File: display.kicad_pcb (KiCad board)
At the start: 2 copper layers, 128.9 x 78.1 mm, 42 parts, among them J8 Screw_Terminal_1x04, U1 LM317T, U2 LM317T

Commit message: Beth's updated copy pre-change
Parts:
- removed B_JACK: BARREL_JACK, new-lib:Barrel_Jack
- removed C1, C3: 0.1micF, Capacitors_THT:CP_Radial_Tantal_D4.5mm_P2.50mm
- removed C2, C4: 1micF, Capacitors_THT:CP_Radial_Tantal_D4.5mm_P2.50mm
- removed Driver-to-LED (x2), Line-input (x2), Row-sink (x2): Screw_Terminal_1x08, Connectors_Terminal_Blocks:TerminalBlock_Pheonix_MPT-2.54mm_8pol
- removed J8: Screw_Terminal_1x04, Connectors_Terminal_Blocks:TerminalBlock_Pheonix_MPT-2.54mm_4pol
- removed R1, R20: 4.7k, Resistors_THT:R_Axial_DIN0204_L3.6mm_D1.6mm_P7.62mm_Horizontal
- removed R10, R11, R12, R13, R14, R15, R16, R17, R18, R21, R22, R3, R4, R5, R6, R7, R8, R9: R, Resistors_THT:R_Axial_DIN0204_L3.6mm_D1.6mm_P7.62mm_Horizontal
- removed R19, R2: 390, Resistors_THT:R_Axial_DIN0204_L3.6mm_D1.6mm_P7.62mm_Horizontal
- removed U1, U2: LM317T, new-lib:LM317T
- added 0.1uF: , Capacitors_THT:C_Disc_D7.5mm_W2.5mm_P5.00mm, F.Cu at (132.0, 97.0)
- added 0.1uF: , Capacitors_THT:C_Disc_D7.5mm_W2.5mm_P5.00mm, F.Cu at (137.0, 97.0)
- added 1uF: , Capacitors_THT:CP_Radial_D5.0mm_P2.00mm, F.Cu at (159.0, 97.0)
- added 1uF: , Capacitors_THT:CP_Radial_D5.0mm_P2.00mm, F.Cu at (149.5, 99.0)
- added 330: R, Resistors_THT:R_Axial_DIN0411_L9.9mm_D3.6mm_P5.08mm_Vertical, F.Cu at (105.6, 84.3)
- added 330: R, Resistors_THT:R_Axial_DIN0411_L9.9mm_D3.6mm_P5.08mm_Vertical, F.Cu at (76.8, 71.6)
- added 330: R, Resistors_THT:R_Axial_DIN0411_L9.9mm_D3.6mm_P5.08mm_Vertical, F.Cu at (79.3, 84.3)
- added 330: R, Resistors_THT:R_Axial_DIN0411_L9.9mm_D3.6mm_P5.08mm_Vertical, F.Cu at (81.9, 71.6)
- added 330: R, Resistors_THT:R_Axial_DIN0411_L9.9mm_D3.6mm_P5.08mm_Vertical, F.Cu at (84.4, 84.3)
- added 330: R, Resistors_THT:R_Axial_DIN0411_L9.9mm_D3.6mm_P5.08mm_Vertical, F.Cu at (87.0, 71.6)
- added 330: R, Resistors_THT:R_Axial_DIN0411_L9.9mm_D3.6mm_P5.08mm_Vertical, F.Cu at (89.5, 84.3)
- added 330: R, Resistors_THT:R_Axial_DIN0411_L9.9mm_D3.6mm_P5.08mm_Vertical, F.Cu at (92.0, 71.6)
- added 330: R, Resistors_THT:R_Axial_DIN0411_L9.9mm_D3.6mm_P5.08mm_Vertical, F.Cu at (100.5, 84.3)
- added 330: R, Resistors_THT:R_Axial_DIN0411_L9.9mm_D3.6mm_P5.08mm_Vertical, F.Cu at (103.1, 71.6)
- added 330: R, Resistors_THT:R_Axial_DIN0411_L9.9mm_D3.6mm_P5.08mm_Vertical, F.Cu at (108.1, 71.6)
- added 330: R, Resistors_THT:R_Axial_DIN0411_L9.9mm_D3.6mm_P5.08mm_Vertical, F.Cu at (110.7, 84.3)
- added 330: R, Resistors_THT:R_Axial_DIN0411_L9.9mm_D3.6mm_P5.08mm_Vertical, F.Cu at (113.2, 71.6)
- added 330: R, Resistors_THT:R_Axial_DIN0411_L9.9mm_D3.6mm_P5.08mm_Vertical, F.Cu at (115.8, 84.3)
- added 330: R, Resistors_THT:R_Axial_DIN0411_L9.9mm_D3.6mm_P5.08mm_Vertical, F.Cu at (118.3, 71.6)
- added 330: R, Resistors_THT:R_Axial_DIN0411_L9.9mm_D3.6mm_P5.08mm_Vertical, F.Cu at (74.3, 84.3)
- added 390: , Resistors_THT:R_Axial_DIN0204_L3.6mm_D1.6mm_P7.62mm_Horizontal, F.Cu at (134.0, 113.9)
- added 390: , Resistors_THT:R_Axial_DIN0204_L3.6mm_D1.6mm_P7.62mm_Horizontal, F.Cu at (126.3, 118.3)
- added 4.7k: , Resistors_THT:R_Axial_DIN0204_L3.6mm_D1.6mm_P7.62mm_Horizontal, F.Cu at (126.3, 109.4)
- added 4.7k: , Resistors_THT:R_Axial_DIN0204_L3.6mm_D1.6mm_P7.62mm_Horizontal, F.Cu at (161.0, 111.5)
- added ?: Screw_Terminal_1x04, Connectors_Terminal_Blocks:TerminalBlock_Pheonix_MPT-2.54mm_4pol, F.Cu at (173.0, 102.5)
- added ?: LM317T, Connectors_Molex:Molex_KK-6410-03_03x2.54mm_Straight, F.Cu at (127.3, 103.5)
- added ?: LM317T, Connectors_Molex:Molex_KK-6410-03_03x2.54mm_Straight, F.Cu at (160.0, 105.5)
- added ?: BARREL_JACK, Connectors:BARREL_JACK, F.Cu at (142.0, 105.5)
- added ?: 3mm drill, Wire_Pads:SolderWirePad_single_2mmDrill, F.Cu at (69.5, 57.5)
- added ?: 3mm drill hole, Wire_Pads:SolderWirePad_single_2mmDrill, F.Cu at (177.5, 57.5)
- added ?: 3mm drill hole, Wire_Pads:SolderWirePad_single_2mmDrill, F.Cu at (177.5, 118.0)
- added ?: 3mm drill hole, Wire_Pads:SolderWirePad_single_2mmDrill, F.Cu at (69.5, 118.0)
- added Driver to LEDs: Screw_Terminal_1x08, Connectors_Terminal_Blocks:TerminalBlock_Pheonix_MPT-2.54mm_8pol, F.Cu at (118.3, 62.7)
- added Driver to LEDs: Screw_Terminal_1x08, Connectors_Terminal_Blocks:TerminalBlock_Pheonix_MPT-2.54mm_8pol, F.Cu at (92.0, 62.7)
- added LEDs to Row Selector: Screw_Terminal_1x08, Connectors_Terminal_Blocks:TerminalBlock_Pheonix_MPT-2.54mm_8pol, F.Cu at (172.5, 62.7)
- added LEDs to Row Selector: Screw_Terminal_1x08, Connectors_Terminal_Blocks:TerminalBlock_Pheonix_MPT-2.54mm_8pol, F.Cu at (145.0, 62.7)
- added R: , Resistors_THT:R_Axial_DIN0204_L3.6mm_D1.6mm_P7.62mm_Horizontal, F.Cu at (153.3, 115.0)
- added R: , Resistors_THT:R_Axial_DIN0204_L3.6mm_D1.6mm_P7.62mm_Horizontal, F.Cu at (161.0, 118.5)
- added REF**: TerminalBlock_Pheonix_PT-3.5mm_2pol, Connectors_Terminal_Blocks:TerminalBlock_Pheonix_PT-3.5mm_2pol, F.Cu at (67.7, 74.8)
- added Register to Driver: Screw_Terminal_1x08, Connectors_Terminal_Blocks:TerminalBlock_Pheonix_MPT-2.54mm_8pol, F.Cu at (100.5, 114.8)
- added Register to Driver: Screw_Terminal_1x08, Connectors_Terminal_Blocks:TerminalBlock_Pheonix_MPT-2.54mm_8pol, F.Cu at (74.3, 114.8)
- moved Driver2 30.5 mm to (100.5, 105.9)
- moved Driver1 27.6 mm to (74.3, 105.9)
- moved Darlington2 16.9 mm to (154.5, 79.5)
- moved Darlington1 16.8 mm to (127.2, 79.5)
- moved Demux1 15.9 mm to (124.7, 90.9)
- moved Demux2 15.2 mm to (152.0, 91.0)
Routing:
- net GND: track 222.0 -> 166.8 mm, vias 0 -> 1
- net Net-(Demux1-Pad3): track 79.3 -> 49.8 mm, vias 2 -> 1
- net Net-(Demux1-Pad5): track 66.9 -> 43.9 mm, vias 3 -> 2
- net Net-(J5-Pad1): track 28.7 -> 8.89 mm
- net Net-(C1-Pad1): track 54.0 -> 35.0 mm
- net Net-(J5-Pad7): track 27.5 -> 8.89 mm
- net Net-(J5-Pad3): track 27.5 -> 8.89 mm
- net Net-(J5-Pad5): track 27.0 -> 8.89 mm
- net Net-(R20-Pad1): track 27.8 -> 10.0 mm, vias 1 -> 0
- net Net-(Driver1-Pad12): track 26.6 -> 8.89 mm
- net Net-(Driver1-Pad14): track 25.7 -> 8.89 mm
- net Net-(Driver1-Pad16): track 25.1 -> 8.89 mm
- net Net-(Driver1-Pad18): track 24.8 -> 8.89 mm
- net Net-(Driver1-Pad15): track 7.52 -> 21.6 mm
- net Net-(Driver1-Pad13): track 8.58 -> 21.6 mm
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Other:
- board size 128.9 x 78.1 mm -> 117 x 69.5 mm
- rule pad_to_mask_clearance: 0.2 -> 0
- board text added: "Produced by Nathan Doorly Beth Cotterell Richard Grafton"
- board text removed: "Designed by Nathan Doorly"

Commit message: Ready for manufacture
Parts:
- removed REF**: TerminalBlock_Pheonix_PT-3.5mm_2pol, Connectors_Terminal_Blocks:TerminalBlock_Pheonix_PT-3.5mm_2pol
- added GND: Screw_Terminal_1x02, Connectors_Terminal_Blocks:TerminalBlock_Pheonix_PT-3.5mm_2pol, F.Cu at (70.5, 71.3)
- 1uF (x2): value (none) -> 1micF
- 390 (x2): value (none) -> 390
- 4.7k (x2): value (none) -> 4.7k
- LED to Column: renamed from Driver to LEDs (x2)
- LED to Row: renamed from LEDs to Row Selector (x2)
- R (x2): value (none) -> R
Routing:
- net GND: track 166.8 -> 214.4 mm
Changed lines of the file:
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@@
 (kicad_pcb (version 4) (host pcbnew 4.0.6)
   (general
-    (links 123)
+    (links 125)
     (no_connects 0)
     (area 64.949999 52.949999 182.050001 122.550001)
     (thickness 1.6)
     (drawings 10)
-    (tracks 306)
+    (tracks 311)
     (zones 0)
     (modules 47)
@@
     (at 118.3 62.7 180)
     (descr "8-way 2.54mm pitch terminal block, Phoenix MPT series")
-    (fp_text reference "Driver to LEDs" (at 8.89 -4.50088 180) (layer F.SilkS)
+    (fp_text reference "LED to Column" (at 8.89 -4.50088 180) (layer F.SilkS)
       (effects (font (size 1 1) (thickness 0.15)))
     )
@@
     (at 92.05 62.7 180)
     (descr "8-way 2.54mm pitch terminal block, Phoenix MPT series")
-    (fp_text reference "Driver to LEDs" (at 8.89 -4.50088 180) (layer F.SilkS)
+    (fp_text reference "LED to Column" (at 8.89 -4.50088 180) (layer F.SilkS)
       (effects (font (size 1 1) (thickness 0.15)))
     )
@@
     (at 172.5 62.7 180)
     (descr "8-way 2.54mm pitch terminal block, Phoenix MPT series")
-    (fp_text reference "LEDs to Row Selector" (at 8.89 -4.50088 180) (layer F.SilkS)
+    (fp_text reference "LED to Row" (at 8.89 -4.50088 180) (layer F.SilkS)
       (effects (font (size 1 1) (thickness 0.15)))
     )
@@
     (at 145 62.7 180)
     (descr "8-way 2.54mm pitch terminal block, Phoenix MPT series")
-    (fp_text reference "LEDs to Row Selector" (at 8.89 -4.50088 180) (layer F.SilkS)
+    (fp_text reference "LED to Row" (at 8.89 -4.50088 180) (layer F.SilkS)
       (effects (font (size 1 1) (thickness 0.15)))
     )
@@
       (effects (font (size 1 1) (thickness 0.15)))
     )
-    (fp_text value "" (at 3.81 1.86) (layer F.Fab)
+    (fp_text value 4.7k (at 3.81 1.86) (layer F.Fab)
       (effects (font (size 1 1) (thickness 0.15)))
     )
@@
       (effects (font (size 1 1) (thickness 0.15)))
     )
-    (fp_text value "" (at 3.5 -1.5 180) (layer F.Fab)
+    (fp_text value 390 (at 3.5 -1.5 180) (layer F.Fab)
       (effects (font (size 1 1) (thickness 0.15)))
     )
@@
       (effects (font (size 1 1) (thickness 0.15)))
     )
-    (fp_text value "" (at 3.81 1.86) (layer F.Fab)
+    (fp_text value 390 (at 3.81 1.86) (layer F.Fab)
       (effects (font (size 1 1) (thickness 0.15)))
     )
@@
       (effects (font (size 1 1) (thickness 0.15)))
     )
-    (fp_text value "" (at 3.81 1.86 180) (layer F.Fab)
+    (fp_text value 4.7k (at 3.81 1.86 180) (layer F.Fab)
       (effects (font (size 1 1) (thickness 0.15)))
     )
@@
       (effects (font (size 1 1) (thickness 0.15)))
     )
-    (fp_text value "" (at 3.5 -1.6) (layer F.Fab)
+    (fp_text value R (at 3.5 -1.6) (layer F.Fab)
       (effects (font (size 1 1) (thickness 0.15)))
     )
@@
       (effects (font (size 1 1) (thickness 0.15)))
     )
-    (fp_text value "" (at 3.81 1.86 180) (layer F.Fab)
+    (fp_text value R (at 3.81 1.86 180) (layer F.Fab)
       (effects (font (size 1 1) (thickness 0.15)))
     )
@@
     (descr "C, Disc series, Radial, pin pitch=5.00mm, , diameter*width=7.5*2.5mm^2, Capacitor, http://www.vishay.com/docs/28535/vy2series.pdf")
     (tags "C Disc series Radial pin pitch 5.00mm  diameter 7.5mm width 2.5mm Capacitor")
-    (fp_text reference 0.1uF (at 3.2 2.2 180) (layer F.SilkS)
-      (effects (font (size 1 1) (thickness 0.15)))
-    )
-    (fp_text value "" (at 2.5 2.56 180) (layer F.Fab)
+    (fp_text reference 0.1uF (at 3.35 2.15 180) (layer F.SilkS)
+      (effects (font (size 1 1) (thickness 0.15)))
+    )
+    (fp_text value "" (at 9.9 2.35 180) (layer F.Fab)
       (effects (font (size 1 1) (thickness 0.15)))
     )
@@
     (fp_line (start 6.6 1.6) (end 6.6 -1.6) (layer F.CrtYd) (width 0.05))
     (fp_line (start 6.6 -1.6) (end -1.6 -1.6) (layer F.CrtYd) (width 0.05))
-    (fp_text user %R (at 2.5 0 180) (layer F.Fab)
+    (fp_text user %R (at 2.4 -2.05 180) (layer F.Fab)
       (effects (font (size 1 1) (thickness 0.15)))
     )
@@
     (descr "C, Disc series, Radial, pin pitch=5.00mm, , diameter*width=7.5*2.5mm^2, Capacitor, http://www.vishay.com/docs/28535/vy2series.pdf")
     (tags "C Disc series Radial pin pitch 5.00mm  diameter 7.5mm width 2.5mm Capacitor")
-    (fp_text reference 0.1uF (at 1.2 -2 180) (layer F.SilkS)
+    (fp_text reference 0.1uF (at 2.7 -2.25) (layer F.SilkS)
       (effects (font (size 1 1) (thickness 0.15)))
     )
@@
     (fp_line (start 6.6 1.6) (end 6.6 -1.6) (layer F.CrtYd) (width 0.05))
     (fp_line (start 6.6 -1.6) (end -1.6 -1.6) (layer F.CrtYd) (width 0.05))
-    (fp_text user %R (at 2.5 0) (layer F.Fab)
+    (fp_text user %R (at 2.5 2.5) (layer F.Fab)
       (effects (font (size 1 1) (thickness 0.15)))
     )
@@
       (effects (font (size 1 1) (thickness 0.15)))
     )
-    (fp_text value "" (at 1 3.81 270) (layer F.Fab)
+    (fp_text value 1micF (at 1 3.81 270) (layer F.Fab)
       (effects (font (size 1 1) (thickness 0.15)))
     )
@@
       (effects (font (size 1 1) (thickness 0.15)))
     )
-    (fp_text value "" (at 1 3.81 90) (layer F.Fab)
+    (fp_text value 1micF (at 1 3.81 90) (layer F.Fab)
       (effects (font (size 1 1) (thickness 0.15)))
     )
@@
   )
   (module Connectors_Terminal_Blocks:TerminalBlock_Pheonix_PT-3.5mm_2pol (layer F.Cu)
-    (at 67.65 74.75)
+    (at 70.55 71.35 270)
     (descr "2-way 3.5mm pitch terminal block, Phoenix PT series")
-    (fp_text reference REF** (at 1.75 -4.3) (layer F.SilkS)
-      (effects (font (size 1 1) (thickness 0.15)))
-    )
-    (fp_text value TerminalBlock_Pheonix_PT-3.5mm_2pol (at 1.75 6) (layer F.Fab)
+    (fp_text reference GND (at -3 1.05 360) (layer F.SilkS)
+      (effects (font (size 1 1) (thickness 0.15)))
+    )
+    (fp_text value Screw_Terminal_1x02 (at 1.75 6 270) (layer F.Fab)
       (effects (font (size 1 1) (thickness 0.15)))
     )
@@
     (fp_line (start 5.25 4.5) (end 5.25 -3.1) (layer F.SilkS) (width 0.15))
     (fp_line (start 5.25 -3.1) (end -1.75 -3.1) (layer F.SilkS) (width 0.15))
-    (pad 2 thru_hole circle (at 3.5 0) (size 2.4 2.4) (drill 1.2) (layers *.Cu *.Mask))
-    (pad 1 thru_hole rect (at 0 0) (size 2.4 2.4) (drill 1.2) (layers *.Cu *.Mask))
+    (pad 2 thru_hole circle (at 3.5 0 270) (size 2.4 2.4) (drill 1.2) (layers *.Cu *.Mask)
+      (net 2 GND))
+    (pad 1 thru_hole rect (at 0 0 270) (size 2.4 2.4) (drill 1.2) (layers *.Cu *.Mask)
+      (net 2 GND))
     (model Terminal_Blocks.3dshapes/TerminalBlock_Pheonix_PT-3.5mm_2pol.wrl
       (at (xyz 0 0 0))
@@
   (segment (start 132 103) (end 132 97) (width 0.25) (layer F.Cu) (net 1) (status 80000))
   (segment (start 132 97) (end 137 97) (width 0.25) (layer B.Cu) (net 1) (status 80000))
+  (segment (start 70.55 74.85) (end 70.55 92.45) (width 0.25) (layer F.Cu) (net 2) (status 400000))
+  (segment (start 91.83 95.5) (end 94.59 98.26) (width 0.25) (layer F.Cu) (net 2) (status 800000))
+  (segment (start 73.6 95.5) (end 91.83 95.5) (width 0.25) (layer F.Cu) (net 2))
+  (segment (start 70.55 92.45) (end 73.6 95.5) (width 0.25) (layer F.Cu) (net 2))
+  (segment (start 70.55 71.35) (end 70.55 74.85) (width 0.25) (layer F.Cu) (net 2) (status C00000))
   (segment (start 133.5 90) (end 134.5 89) (width 0.25) (layer B.Cu) (net 2))
   (segment (start 140.5 89) (end 141.5 90) (width 0.25) (layer B.Cu) (net 2))

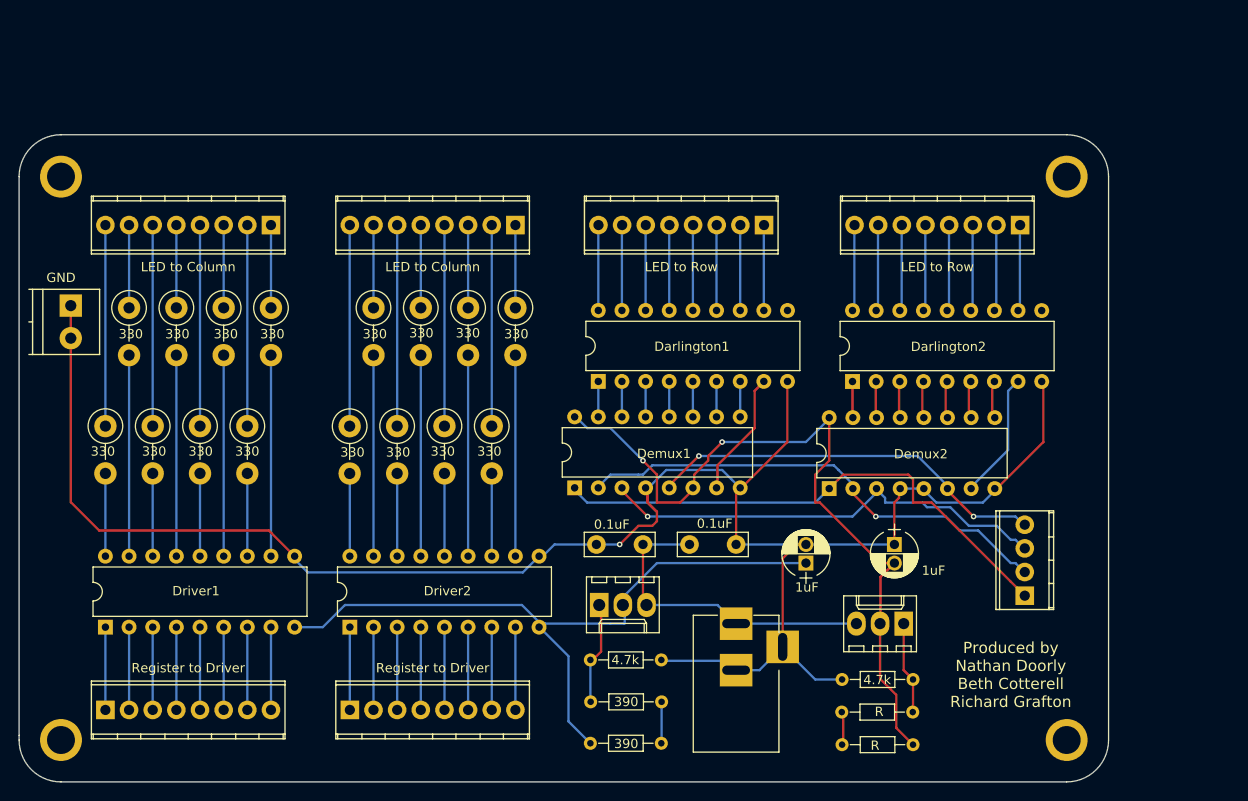
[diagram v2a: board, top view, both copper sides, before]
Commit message: Updated spacing, values and hole sizes
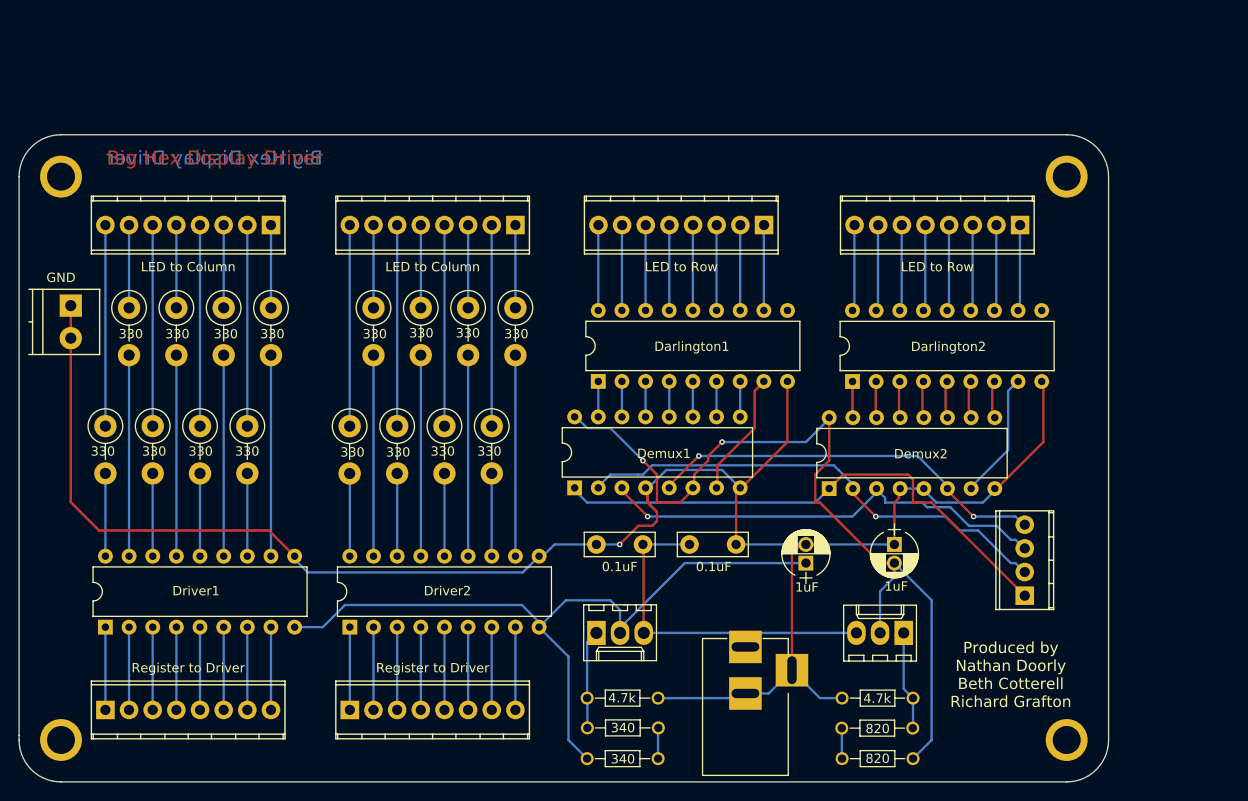
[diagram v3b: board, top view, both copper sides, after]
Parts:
- moved 4.7k 4.11 mm to (126.0, 113.5)
- moved ? 3.01 mm to (127.0, 106.5)
- moved 340 2.82 mm to (133.7, 116.7)
- moved ? 2.69 mm to (143.0, 108.0)
- moved 4.7k 2.00 mm to (161.0, 113.5)
- moved 820 1.72 mm to (153.3, 116.7)
- moved 340 1.69 mm to (126.0, 120.0)
- moved 820 1.50 mm to (161.0, 120.0)
- moved ? 1.00 mm to (160.0, 106.5)
- renumbered 390 to 340, R to 820
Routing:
- net +5V: track 81.2 -> 91.2 mm
- net +9V: track 77.3 -> 82.5 mm
- net Net-(C1-Pad1): track 35.0 -> 38.6 mm
- net GND: track 214.4 -> 216.3 mm
- net Net-(R19-Pad2): track 4.46 -> 3.31 mm
- net Net-(R20-Pad1): track 10.0 -> 10.7 mm
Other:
- board text added: "Big Hex Display Driver"
